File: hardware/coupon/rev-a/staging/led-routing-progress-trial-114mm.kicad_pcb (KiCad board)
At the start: 6 copper layers, 114 x 32.5 mm, 483 parts, among them J1 USB4505-03-0-A, J2 S2B-PH-SM4-TB, SW1 EVQP7J01P, SW2 JS202011JCQN, U1 TLC59581RTQT, U11 SN74LVC1G04DBVR, U17 SN74LVC1G11DBVR, U2 74HC4514PW,118, U23 SN74LVC1G06DBVR, U24 SN74LVC2G17DBVR, U25 SN74LVC2G17DBVR, U29 TPS70933DBVR, U3 ESP32-S3-WROOM-1U-N16R8, U31 TUSB320LAIRWBR, U32 TS3USB31ERSER, U33 TPD4E05U06DQAR, U34 TPS3808G01DBVR, U35 MAX17048G+T10, U36 TPS631000DRLR, U37 TPS63020DSJT, U38 2.5V shunt, U39 TMP390A2DRLR, U40 SN74AUP1G125DBVR, U41 BQ24074RGTR, U42 SN74AUP1G125DBVR, U43 SN74AUP1G125DBVR, U44 TPS259474ARPWR, U45 TPS259474ARPWR, U46 TCA9517ADGKR, U47 TPS3823A-33DBVR, U48 SN74LVC1G04DSFR, U49 SN74LVC1G74RSER, U50 SN74LVC1G74RSER, U51 SN74LVC1G11DRYR, U52 SN74LVC1G08DSFR, U53 TLV6700DSER, U54 SN74LVC2G00DCUR, U55 SN74LVC2G08DCUR

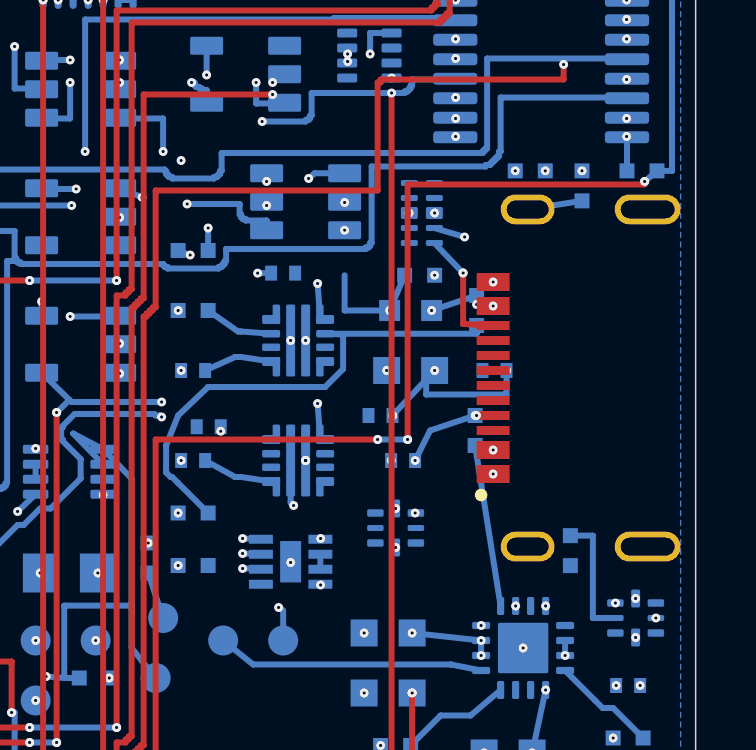
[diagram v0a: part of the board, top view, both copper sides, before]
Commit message: Connect connector-facing USB data groups at 76 opens
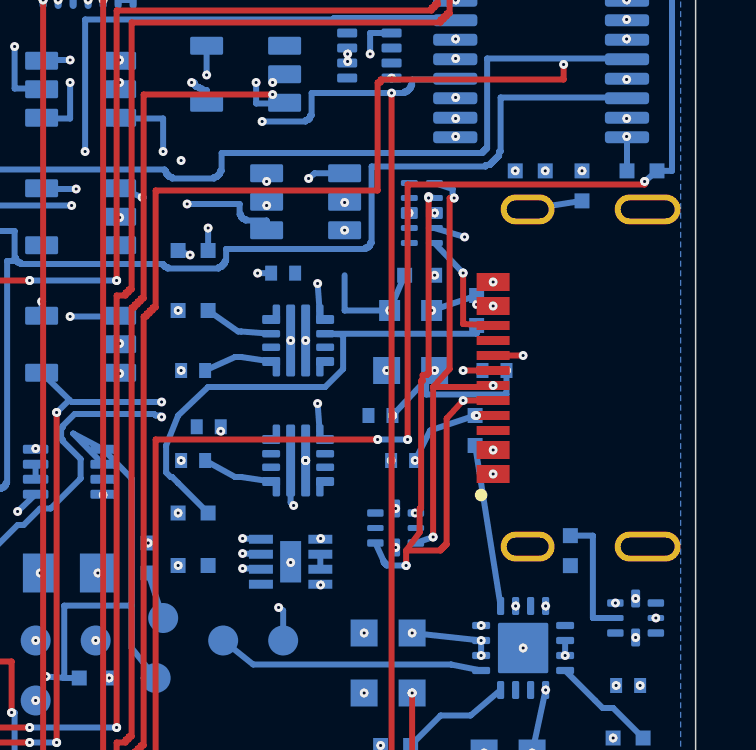
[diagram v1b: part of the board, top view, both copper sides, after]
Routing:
- net USB_CONN_DM: track 0.00 -> 24.1 mm, vias 0 -> 12
- net USB_CONN_DP: track 0.00 -> 18.3 mm, vias 0 -> 12
